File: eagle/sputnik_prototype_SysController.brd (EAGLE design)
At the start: 100 x 80 mm, 23 parts, among them U1 MEGA128-M, U2 MIC5219 3.3V, Y2 8MHZ

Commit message: Added GPIOs and other updates on SysCon sch. Updated SPI cache footprint
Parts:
- removed JP4: (no value), pinhead:1_05X2MM
- added JP6, JP7, JP8: (no value), psas_c3_team05:2X10
- added TP15, TP16, TP17, TP18, TP19, TP2, TP20, TP21, TP22, TP23, TP24, TP25, TP26, TP27, TP3, TP6, TP7, TP8, TP9: TPSPAD1-13, testpad:P1-13
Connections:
- net PTA1/UART0RX renamed PTA1/UART0_RX
- net PTA2/UART0TX renamed PTA2/UART0_TX
- net PTA20/!RESET renamed PTA20/RESET
- new net PA0: JP6.17, JP6.18, TP6.TP, U1.51
- new net PA1: JP6.15, JP6.16, TP3.TP, U1.50
- new net PA2: JP6.13, JP6.14, TP2.TP, U1.49
- new net PB0: JP7.17, JP7.18, TP19.TP, U1.10
- new net PB1: JP7.15, JP7.16, TP18.TP, U1.11
- new net PB2: JP7.13, JP7.14, TP17.TP, U1.12
- new net PB3: JP7.11, JP7.12, TP16.TP, U1.13
- new net PB4: JP7.10, JP7.9, TP15.TP, U1.14
- new net PB5: JP7.7, JP7.8, TP9.TP, U1.15
- new net PB6: JP7.5, JP7.6, TP8.TP, U1.16
- new net PB7: JP7.3, JP7.4, TP7.TP, U1.17
- new net PC0: JP8.17, JP8.18, TP27.TP, U1.35
- new net PC1: JP8.15, JP8.16, TP26.TP, U1.36
- new net PC2: JP8.13, JP8.14, TP25.TP, U1.37
- new net PC3: JP8.11, JP8.12, TP24.TP, U1.38
- new net PC4: JP8.10, JP8.9, TP23.TP, U1.39
- new net PC5: JP8.7, JP8.8, TP22.TP, U1.40
- new net PC6: JP8.5, JP8.6, TP21.TP, U1.41
- new net PC7: JP8.3, JP8.4, TP20.TP, U1.42
- net GND: now also JP6.19, JP6.20, JP7.19, JP7.20, JP8.19, JP8.20
- net PA3: now also JP6.11, JP6.12, TP14.TP; no longer JP4.1, TP10.TP
- net PA4: now also JP6.10, JP6.9, TP13.TP; no longer JP4.2, TP11.TP
- net PA5: now also JP6.7, JP6.8; no longer JP4.3
- net PA6: now also JP6.5, JP6.6, TP11.TP; no longer JP4.4, TP13.TP
- net PA7: now also JP6.3, JP6.4, TP10.TP; no longer JP4.5, TP14.TP
- net UART1_RX: now also U1.27
- net UART1_TX: now also U1.28
- net V+: now also JP6.1, JP6.2, JP7.1, JP7.2, JP8.1, JP8.2

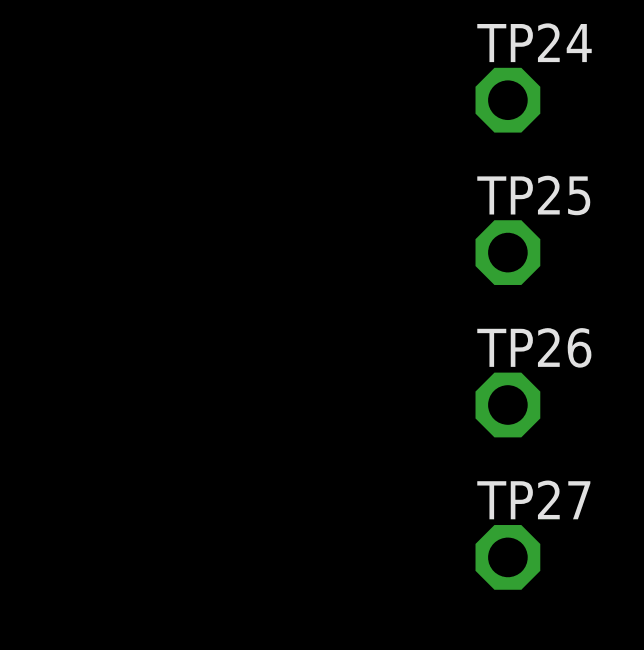
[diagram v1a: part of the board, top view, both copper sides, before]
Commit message: Added super cap and LDO holding place
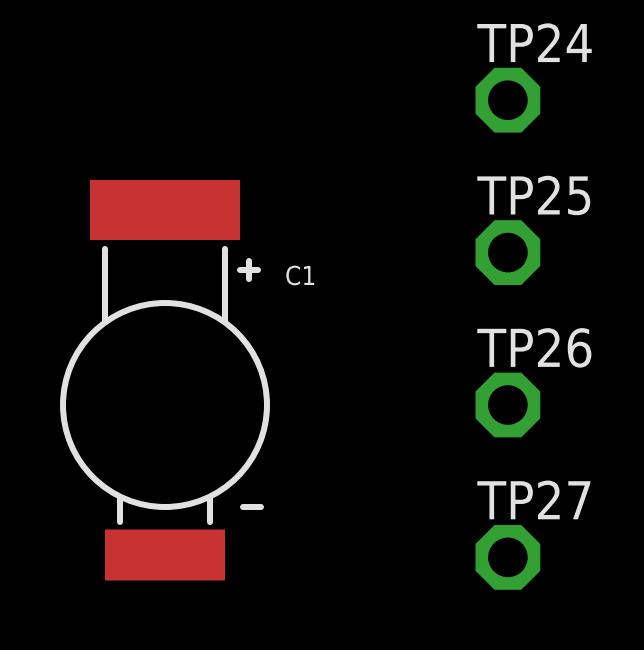
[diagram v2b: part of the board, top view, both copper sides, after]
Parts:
- added C1: CAP-ELNA-DS, cap-elna-ds:CAP-ELNA-DS-SERIES
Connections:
- net 3.3V: now also C1.+
- net GND: now also C1.-
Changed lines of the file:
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@@
 <layer number="56" name="wert" color="7" fill="1" visible="no" active="no"/>
 <layer number="57" name="tCAD" color="7" fill="1" visible="no" active="no"/>
+<layer number="59" name="Invisible" color="7" fill="1" visible="no" active="no"/>
+<layer number="61" name="stand" color="7" fill="1" visible="no" active="no"/>
 <layer number="90" name="Modules" color="5" fill="1" visible="no" active="no"/>
 <layer number="91" name="Nets" color="2" fill="1" visible="no" active="no"/>
@@
 <layer number="127" name="_tValues" color="7" fill="1" visible="yes" active="yes"/>
 <layer number="128" name="_bValues" color="7" fill="1" visible="yes" active="yes"/>
+<layer number="130" name="bLogo" color="7" fill="1" visible="yes" active="yes"/>
 <layer number="131" name="tAdjust" color="7" fill="1" visible="yes" active="yes"/>
 <layer number="132" name="bAdjust" color="7" fill="1" visible="yes" active="yes"/>
@@
 <layer number="223" name="223bmp" color="7" fill="1" visible="yes" active="yes"/>
 <layer number="224" name="224bmp" color="7" fill="1" visible="yes" active="yes"/>
+<layer number="225" name="225bmp" color="7" fill="1" visible="yes" active="yes"/>
+<layer number="226" name="226bmp" color="7" fill="1" visible="yes" active="yes"/>
+<layer number="227" name="227bmp" color="7" fill="1" visible="yes" active="yes"/>
+<layer number="228" name="228bmp" color="7" fill="1" visible="yes" active="yes"/>
 <layer number="231" name="Eagle3D_PG1" color="7" fill="1" visible="yes" active="yes"/>
 <layer number="232" name="Eagle3D_PG2" color="7" fill="1" visible="yes" active="yes"/>
@@
 <attribute name="TP_SIGNAL_NAME" value="" x="-55.88" y="-227.33" size="1.778" layer="27" display="off"/>
 </element>
+<element name="C1" library="cap-elna-ds" package="CAP-ELNA-DS-SERIES" value="CAP-ELNA-DS" x="-67.31" y="-222.25"/>
 </elements>
 <signals>
@@
 <contactref element="JP6" pad="19"/>
 <contactref element="JP6" pad="20"/>
+<contactref element="C1" pad="-"/>
 <wire x1="-56.68" y1="-101.6" x2="-56.68" y2="-106.68" width="0" layer="19" extent="1-1"/>
 <wire x1="-56.68" y1="-96.52" x2="-56.68" y2="-101.6" width="0" layer="19" extent="1-1"/>
@@
 <wire x1="-42.71" y1="36.83" x2="-37.63" y2="36.83" width="0" layer="19" extent="1-1"/>
 <wire x1="-53.34" y1="36.83" x2="-42.71" y2="36.83" width="0" layer="19" extent="1-1"/>
+<wire x1="-67.31" y1="-227.25" x2="-33.02" y2="-130.81" width="0" layer="19" extent="1-1"/>
 </signal>
 <signal name="V+">
@@
 <contactref element="U2" pad="5"/>
 <contactref element="TP1" pad="TP"/>
+<contactref element="C40" pad="2"/>
 <contactref element="U1" pad="52"/>
-<contactref element="C39" pad="2"/>
-<contactref element="JP3" pad="4"/>
-<contactref element="JP3" pad="7"/>
-<contactref element="C36" pad="2"/>
 <contactref element="U1" pad="62"/>
 <contactref element="U1" pad="21"/>
+<contactref element="C36" pad="2"/>
 <contactref element="C37" pad="2"/>
 <contactref element="U1" pad="64"/>
+<contactref element="C39" pad="2"/>
 <contactref element="C38" pad="2"/>
-<contactref element="C40" pad="2"/>
+<contactref element="JP3" pad="7"/>
+<contactref element="JP3" pad="4"/>
+<contactref element="C1" pad="+"/>
 <wire x1="-55.88" y1="-21.59" x2="-55.08" y2="-96.52" width="0" layer="19" extent="1-1"/>
 <wire x1="-58.1" y1="-15.2099" x2="-55.88" y2="-21.59" width="0" layer="19" extent="1-1"/>
@@
 <wire x1="-36.03" y1="36.83" x2="-30.95" y2="36.83" width="0" layer="19" extent="1-1"/>
 <wire x1="-41.11" y1="36.83" x2="-36.03" y2="36.83" width="0" layer="19" extent="1-1"/>
+<wire x1="-67.31" y1="-215.75" x2="-55.08" y2="-96.52" width="0" layer="19" extent="1-1"/>
 </signal>
 <signal name="N$3">

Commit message: Added rad-hard model LDO
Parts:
- removed C40: 2.2uF, rcl_custom:.0603-B-NOSILK
- removed C41: 100nF, rcl_custom:.0603-B-NOSILK
- removed C42: 470pF, rcl_custom:.0603-B-NOSILK
- removed TP1: TPSPAD1-13, testpad:P1-13
- removed U2: MIC5219 3.3V, Lilypad_Arduino_USB_v12:SPARKFUN-POWERIC_SOT23-5
- added C2, C3, C4, C43: (no value), rcl:CT6032
- added R1, R2, R3, R4, R5: (no value), rcl_custom:.0603-B-NOSILK
- added U$1: TPS7H1201-HT, psas_c3_team05:TPS7H1201-HT
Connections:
- removed net 3.3V: C1.+, C36.2, C37.2, C38.2, C39.2, C40.2, JP3.4, JP3.7, TP1.TP, U1.21, U1.52, U1.62, U1.64, U2.5
- new net N$1: C36.2, C37.2, C38.2, C39.2, C4.-, JP3.4, JP3.7, R4.2, R5.2, U$1.11, U$1.12, U$1.13, U$1.14, U1.21, U1.52, U1.62, U1.64
- new net N$2: C43.+, U$1.1
- new net N$4: C3.+, U$1.16
- new net N$5: C4.+, U$1.15
- new net N$6: R3.2, R4.1
- new net N$7: R5.1, U$1.9
- new net N$8: R2.2, U$1.7
- new net N$9: R1.1, U$1.10
- net GND: now also C2.-, C3.-, C43.-, R2.1, R3.1, U$1.8; no longer C40.1, C41.1, C42.1, U2.2
- net N$3: now also C1.+, C2.+, R1.2, U$1.3, U$1.4, U$1.5, U$1.6; no longer C42.2, U2.4
- net V+: no longer C41.2, U2.1, U2.3

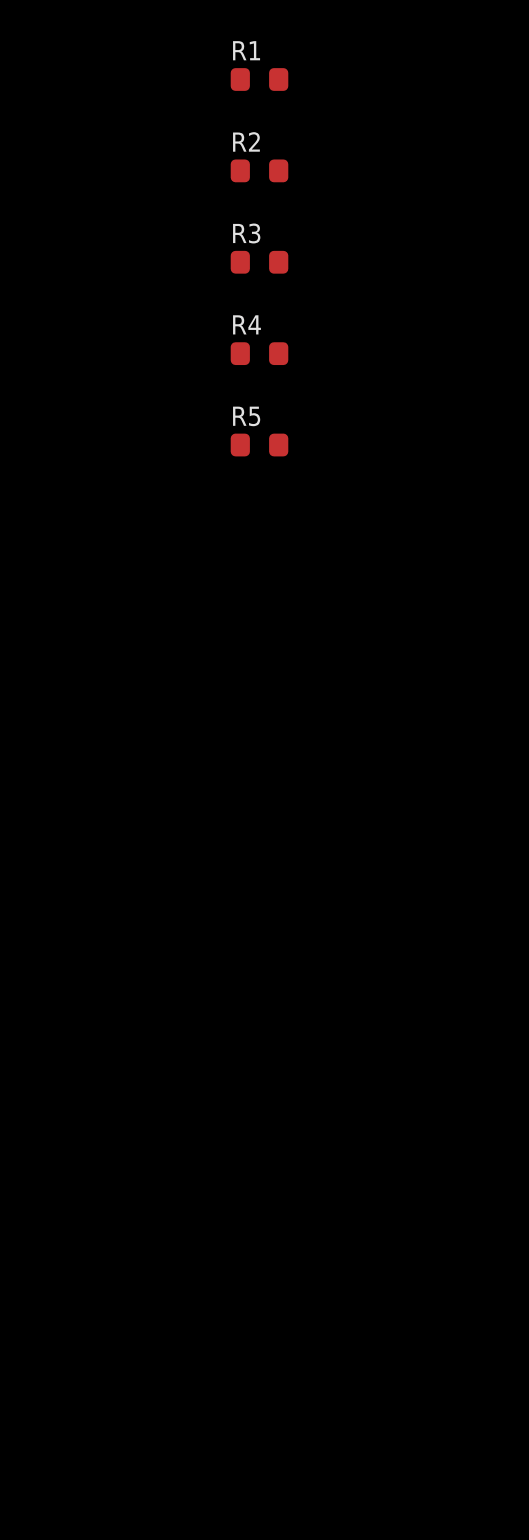
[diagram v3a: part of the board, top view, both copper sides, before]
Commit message: Added optocoupler datasheet and into the schematic
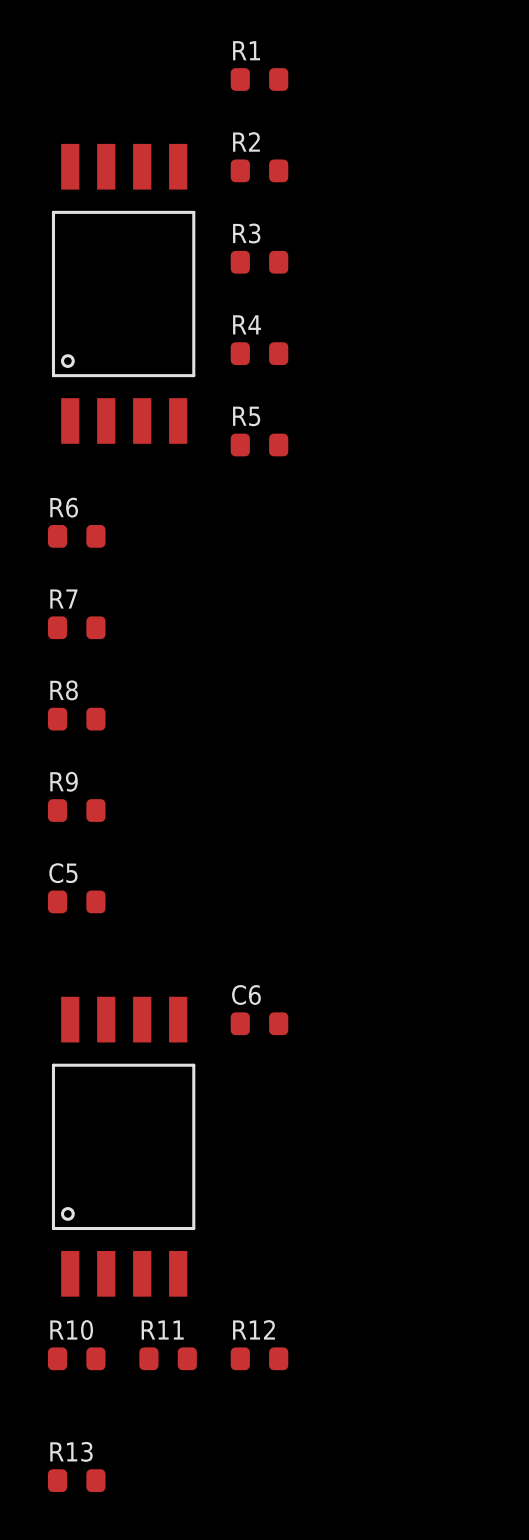
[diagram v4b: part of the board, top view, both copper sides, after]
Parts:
- added C5, C6: 0.1uF, rcl_custom:.0603-B-NOSILK
- added R10, R11, R12, R13, R6, R7, R8, R9: 390, rcl_custom:.0603-B-NOSILK
- added U$2, U$3: ACPL-064L/K64L, psas_c3_team05:ACPL-064L/K64L
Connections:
- removed net PTA1/UART0_RX: U1.3
- removed net PTA2/UART0_TX: U1.2
- new net N$10: R6.2, U1.28
- new net N$16: R9.2, U1.27
- new net N$18: R6.1, U$2.1
- new net N$19: R7.1, U$2.2
- new net N$20: R8.1, U$2.3
- new net N$21: R9.1, U$2.4
- new net N$26: R10.1, U$3.1
- new net N$27: R11.1, U$3.2
- new net N$28: R12.1, U$3.3
- new net N$29: R13.1, U$3.4
- new net PTA1: R10.2, U1.3
- new net PTA2: R13.2, U1.2
- new net UART0_RX: U$3.7
- new net UART0_TX: U$3.6
- net GND: now also C5.1, C6.1, R11.2, R12.2, R7.2, R8.2, U$2.5, U$3.5
- net UART1_RX: now also U$2.6; no longer U1.27
- net UART1_TX: now also U$2.7; no longer U1.28
- net V+: now also C5.2, C6.2, U$2.8, U$3.8
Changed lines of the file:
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@@
 <element name="R4" library="rcl_custom" package=".0603-B-NOSILK" value="" x="-68.58" y="-298.45"/>
 <element name="R5" library="rcl_custom" package=".0603-B-NOSILK" value="" x="-68.58" y="-302.26"/>
+<element name="U$2" library="psas_c3_team05" package="ACPL-064L/K64L" value="ACPL-064L/K64L" x="-77.47" y="-289.56"/>
+<element name="R6" library="rcl_custom" package=".0603-B-NOSILK" value="390" x="-76.2" y="-306.07"/>
+<element name="R7" library="rcl_custom" package=".0603-B-NOSILK" value="390" x="-76.2" y="-309.88"/>
+<element name="R8" library="rcl_custom" package=".0603-B-NOSILK" value="390" x="-76.2" y="-313.69"/>
+<element name="R9" library="rcl_custom" package=".0603-B-NOSILK" value="390" x="-76.2" y="-317.5"/>
+<element name="C5" library="rcl_custom" package=".0603-B-NOSILK" value="0.1uF" x="-76.2" y="-321.31"/>
+<element name="U$3" library="psas_c3_team05" package="ACPL-064L/K64L" value="ACPL-064L/K64L" x="-77.47" y="-325.12"/>
+<element name="R10" library="rcl_custom" package=".0603-B-NOSILK" value="390" x="-76.2" y="-340.36"/>
+<element name="R11" library="rcl_custom" package=".0603-B-NOSILK" value="390" x="-72.39" y="-340.36"/>
+<element name="R12" library="rcl_custom" package=".0603-B-NOSILK" value="390" x="-68.58" y="-340.36"/>
+<element name="R13" library="rcl_custom" package=".0603-B-NOSILK" value="390" x="-76.2" y="-345.44"/>
+<element name="C6" library="rcl_custom" package=".0603-B-NOSILK" value="0.1uF" x="-68.58" y="-326.39"/>
 </elements>
 <signals>
@@
 <contactref element="C38" pad="1"/>
 <contactref element="Y2" pad="2"/>
+<contactref element="R8" pad="2"/>
+<contactref element="R7" pad="2"/>
+<contactref element="U$2" pad="5"/>
+<contactref element="C5" pad="1"/>
+<contactref element="R11" pad="2"/>
+<contactref element="R12" pad="2"/>
+<contactref element="U$3" pad="5"/>
+<contactref element="C6" pad="1"/>
 <wire x1="-33.02" y1="-128.27" x2="-33.02" y2="-130.81" width="0" layer="19" extent="1-1"/>
 <wire x1="-33.02" y1="-123.19" x2="-33.02" y2="-128.27" width="0" layer="19" extent="1-1"/>
@@
 <wire x1="-63.54" y1="-275.59" x2="-63.54" y2="-269.24" width="0" layer="19" extent="1-1"/>
 <wire x1="-69.38" y1="-290.83" x2="-63.54" y2="-275.59" width="0" layer="19" extent="1-1"/>
+<wire x1="-71.97" y1="-290.6575" x2="-69.38" y2="-290.83" width="0" layer="19" extent="1-1"/>
 <wire x1="-69.38" y1="-294.64" x2="-69.38" y2="-290.83" width="0" layer="19" extent="1-1"/>
+<wire x1="-75.4" y1="-309.88" x2="-69.38" y2="-294.64" width="0" layer="19" extent="1-1"/>
+<wire x1="-75.4" y1="-313.69" x2="-75.4" y2="-309.88" width="0" layer="19" extent="1-1"/>
+<wire x1="-77" y1="-321.31" x2="-75.4" y2="-313.69" width="0" layer="19" extent="1-1"/>
+<wire x1="-71.97" y1="-326.2175" x2="-77" y2="-321.31" width="0" layer="19" extent="1-1"/>
+<wire x1="-69.38" y1="-326.39" x2="-71.97" y2="-326.2175" width="0" layer="19" extent="1-1"/>
+<wire x1="-67.78" y1="-340.36" x2="-69.38" y2="-326.39" width="0" layer="19" extent="1-1"/>
+<wire x1="-71.59" y1="-340.36" x2="-67.78" y2="-340.36" width="0" layer="19" extent="1-1"/>
 <wire x1="-30.48" y1="6.35" x2="-33.02" y2="-113.03" width="0" layer="19" extent="1-1"/>
 <wire x1="-40.64" y1="6.35" x2="-30.48" y2="6.35" width="0" layer="19" extent="1-1"/>
@@
 <contactref element="JP6" pad="2"/>
 <contactref element="JP6" pad="1"/>
+<contactref element="U$2" pad="8"/>
+<contactref element="C5" pad="2"/>
+<contactref element="U$3" pad="8"/>
+<contactref element="C6" pad="2"/>
 <wire x1="-55.88" y1="-128.27" x2="-55.88" y2="-130.81" width="0" layer="19" extent="1-1"/>
 <wire x1="-55.88" y1="-123.19" x2="-55.88" y2="-128.27" width="0" layer="19" extent="1-1"/>
@@
 <wire x1="-55.88" y1="-113.03" x2="-55.88" y2="-115.57" width="0" layer="19" extent="1-1"/>
 <wire x1="-17.78" y1="25.4" x2="-55.88" y2="-113.03" width="0" layer="19" extent="1-1"/>
+<wire x1="-76.47" y1="-290.6575" x2="-55.88" y2="-130.81" width="0" layer="19" extent="1-1"/>
+<wire x1="-75.4" y1="-321.31" x2="-76.47" y2="-290.6575" width="0" layer="19" extent="1-1"/>
+<wire x1="-76.47" y1="-326.2175" x2="-75.4" y2="-321.31" width="0" layer="19" extent="1-1"/>
+<wire x1="-67.78" y1="-326.39" x2="-76.47" y2="-326.2175" width="0" layer="19" extent="1-1"/>
 </signal>
 <signal name="SDL">
@@
 </signal>
 <signal name="UART1_RX">
-<contactref element="U1" pad="27"/>
 <contactref element="JP5" pad="1"/>
 <contactref element="TP4" pad="TP"/>
+<contactref element="U$2" pad="6"/>
+<wire x1="-55.88" y1="-36.83" x2="-73.47" y2="-290.6575" width="0" layer="19" extent="1-1"/>
 <wire x1="-53.34" y1="-3.81" x2="-55.88" y2="-36.83" width="0" layer="19" extent="1-1"/>
-<wire x1="-20.34" y1="13.455" x2="-53.34" y2="-3.81" width="0" layer="19" extent="1-1"/>
 </signal>
 <signal name="UART1_TX">
-<contactref element="U1" pad="28"/>
 <contactref element="JP5" pad="2"/>
 <contactref element="TP5" pad="TP"/>
+<contactref element="U$2" pad="7"/>
+<wire x1="-55.88" y1="-41.91" x2="-74.97" y2="-290.6575" width="0" layer="19" extent="1-1"/>
 <wire x1="-50.8" y1="-3.81" x2="-55.88" y2="-41.91" width="0" layer="19" extent="1-1"/>
-<wire x1="-19.84" y1="13.455" x2="-50.8" y2="-3.81" width="0" layer="19" extent="1-1"/>
 </signal>
 <signal name="PA2">
@@
 <wire x1="-17.265" y1="15.03" x2="-35.56" y2="-128.27" width="0" layer="19" extent="1-1"/>
 </signal>
-<signal name="PTA2/UART0_TX">
+<signal name="PTA2">
 <contactref element="U1" pad="2"/>
-</signal>
-<signal name="PTA1/UART0_RX">
+<contactref element="R13" pad="2"/>
+<wire x1="-25.915" y1="21.03" x2="-75.4" y2="-345.44" width="0" layer="19" extent="1-1"/>
+</signal>
+<signal name="PTA1">
 <contactref element="U1" pad="3"/>
+<contactref element="R10" pad="2"/>
+<wire x1="-25.915" y1="20.53" x2="-75.4" y2="-340.36" width="0" layer="19" extent="1-1"/>
 </signal>
 <signal name="PTA20/RESET">
@@
 <wire x1="-67.31" y1="-215.75" x2="-56.13" y2="-232.05" width="0" layer="19" extent="1-1"/>
 </signal>
+<signal name="N$10">
+<contactref element="U1" pad="28"/>
+<contactref element="R6" pad="2"/>
+<wire x1="-19.84" y1="13.455" x2="-75.4" y2="-306.07" width="0" layer="19" extent="1-1"/>
+</signal>
+<signal name="N$16">
+<contactref element="U1" pad="27"/>
+<contactref element="R9" pad="2"/>
+<wire x1="-20.34" y1="13.455" x2="-75.4" y2="-317.5" width="0" layer="19" extent="1-1"/>
+</signal>
+<signal name="N$18">
+<contactref element="R6" pad="1"/>
+<contactref element="U$2" pad="1"/>
+<wire x1="-76.47" y1="-301.2575" x2="-77" y2="-306.07" width="0" layer="19" extent="1-1"/>
+</signal>
+<signal name="N$19">
+<contactref element="R7" pad="1"/>
+<contactref element="U$2" pad="2"/>
+<wire x1="-74.97" y1="-301.2575" x2="-77" y2="-309.88" width="0" layer="19" extent="1-1"/>
+</signal>
+<signal name="N$20">
+<contactref element="R8" pad="1"/>
+<contactref element="U$2" pad="3"/>
+<wire x1="-73.47" y1="-301.2575" x2="-77" y2="-313.69" width="0" layer="19" extent="1-1"/>
+</signal>
+<signal name="N$21">
+<contactref element="R9" pad="1"/>
+<contactref element="U$2" pad="4"/>
+<wire x1="-71.97" y1="-301.2575" x2="-77" y2="-317.5" width="0" layer="19" extent="1-1"/>
+</signal>
+<signal name="UART0_TX">
+<contactref element="U$3" pad="6"/>
+</signal>
+<signal name="UART0_RX">
+<contactref element="U$3" pad="7"/>
+</signal>
+<signal name="N$26">
+<contactref element="R10" pad="1"/>
+<contactref element="U$3" pad="1"/>
+<wire x1="-76.47" y1="-336.8175" x2="-77" y2="-340.36" width="0" layer="19" extent="1-1"/>
+</signal>
+<signal name="N$27">
+<contactref element="R11" pad="1"/>
+<contactref element="U$3" pad="2"/>
+<wire x1="-74.97" y1="-336.8175" x2="-73.19" y2="-340.36" width="0" layer="19" extent="1-1"/>
+</signal>
+<signal name="N$28">
+<contactref element="R12" pad="1"/>
+<contactref element="U$3" pad="3"/>
+<wire x1="-73.47" y1="-336.8175" x2="-69.38" y2="-340.36" width="0" layer="19" extent="1-1"/>
+</signal>
+<signal name="N$29">
+<contactref element="R13" pad="1"/>
+<contactref element="U$3" pad="4"/>
+<wire x1="-71.97" y1="-336.8175" x2="-77" y2="-345.44" width="0" layer="19" extent="1-1"/>
+</signal>
 </signals>

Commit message: added attributes, replaced atmega footprint with correct version, replaced resonator with xtal
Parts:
- removed Y2: 8MHZ, Lilypad_Arduino_USB_v12:SPARKFUN-FREQCTRL_RESONATOR-SMD
- added C7, C8: 9pF, rcl_custom:.0603-B-NOSILK
- added X1: (no value), monitor-v2:CRYSTAL-3.2X1.5-A
- U1: value MEGA128-M -> MEGA128-A; device atmel:MLF64-TH -> atmel:TQFP64
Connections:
- removed net N$23: U1.23, Y2.1
- removed net N$36: U1.24, Y2.3
- new net N$17: C7.2, U1.23, X1.1
- new net N$22: C8.2, U1.24, X1.2
- net GND: now also C7.1, C8.1; no longer U1.TH, Y2.2
